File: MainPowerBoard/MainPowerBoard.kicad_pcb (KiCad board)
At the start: 2 copper layers, 177.8 x 177.8 mm, 255 parts, among them J101 CONN_01X04, J102 CONN_01X04, J103 CONN_01X04, J104 CONN_01X02, J105 CONN_01X02, J106 CONN_01X06, J107 CONN_01X06, J108 CONN_01X04, J109 CONN_01X04, J110 CONN_01X02, J111 CONN_01X02, J112 CONN_01X02, J113 CONN_01X02, J114 CONN_01X02, J115 CONN_01X02, J116 CONN_01X02, J117 CONN_01X02, J118 CONN_01X02, J119 CONN_01X02, J120 CONN_01X02, J121 CONN_01X02, J122 CONN_01X02, J123 CONN_01X02, J124 CONN_01X02, J125 CONN_01X02, J126 CONN_01X02, J127 CONN_01X04, J130 MOUNTING_HOLE, J131 MOUNTING_HOLE, J132 MOUNTING_HOLE, J133 MOUNTING_HOLE, Q101 FDB3632, Q401 FDB3632, Q501 FDB3632, Q601 FDB3632, SW701 KS-01Q-01, U1001 LMR16030S, U101 LTC4357MPMS8, U1101 LMR16030S, U1201 LMR16030S, U1301 LMR16030S, U1401 LMR16030S, U201 LMR16030S, U301 LMR16030S, U401 LTC4357MPMS8, U501 LTC4357MPMS8, U601 LTC4357MPMS8, U701 AP2204RA-5.0TRG1, U702 TLV271IDBVR, U703 LTC2950-1, U704 TLC393, U801 LMR16030S, U901 LMR16030S

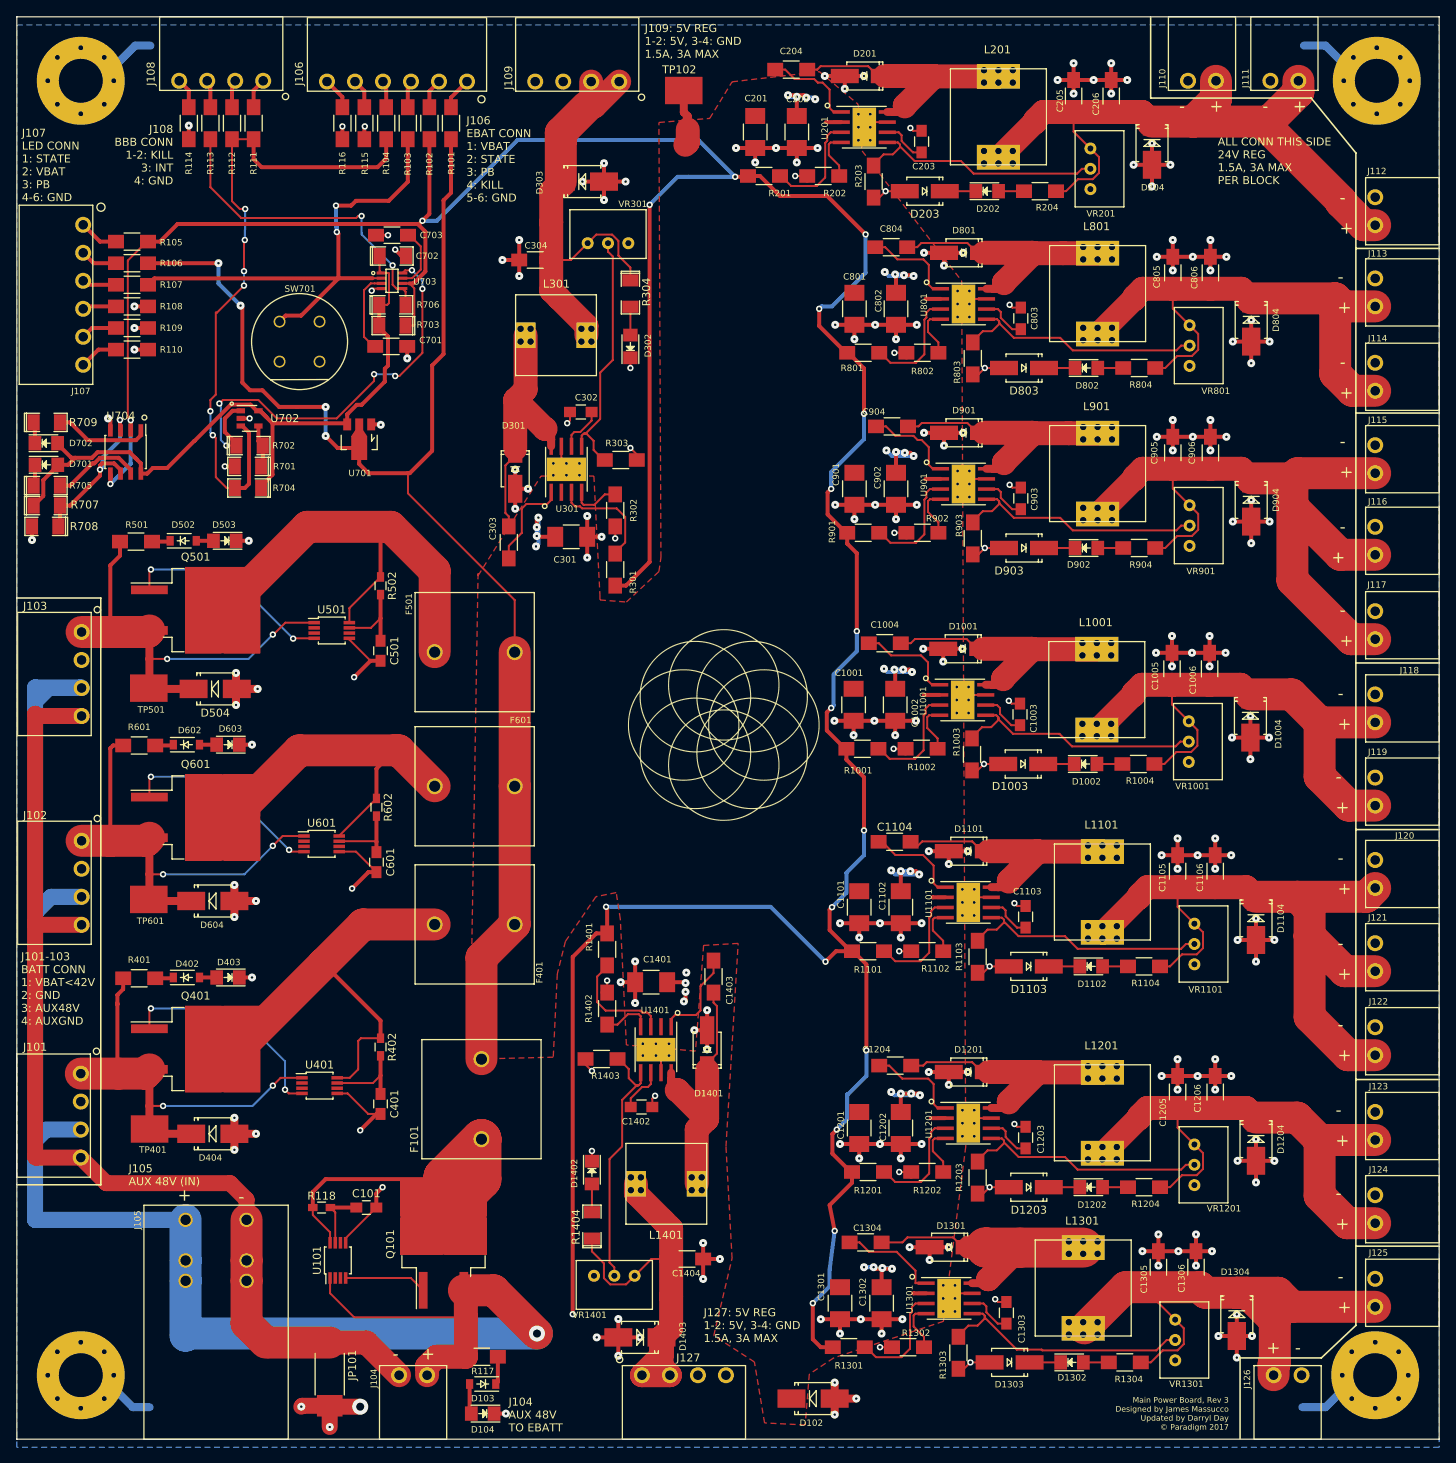
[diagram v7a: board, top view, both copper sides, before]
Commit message: Converted back to 8 24V rails on MPB, fixed NC pins on THBO schematic
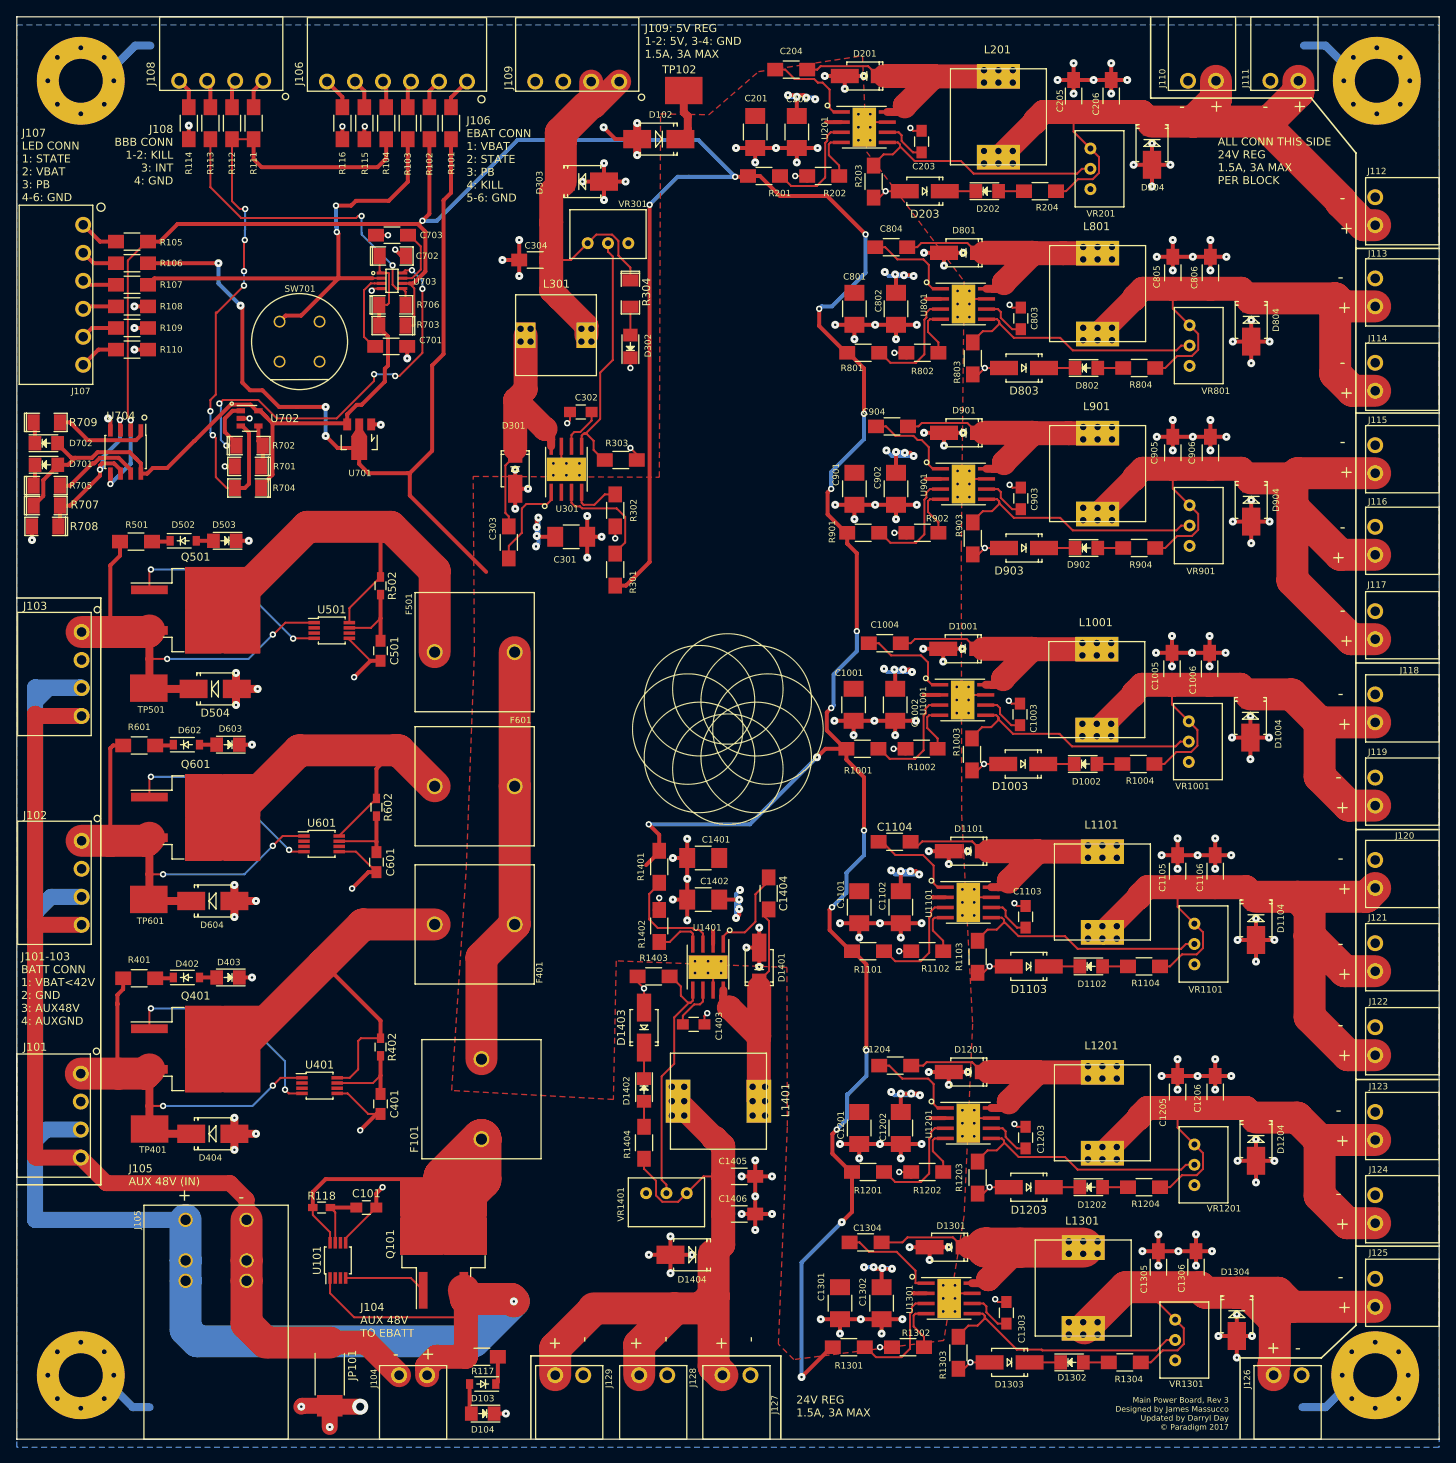
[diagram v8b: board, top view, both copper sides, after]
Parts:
- added C1405: 4.7uF, Capacitors_SMD:C_1206_HandSoldering, F.Cu at (90.3, 144.9)
- added C1406: 4.7uF, Capacitors_SMD:C_1206_HandSoldering, F.Cu at (90.3, 149.6)
- added D1404: 28V, Diodes_SMD:SMB_Handsoldering, F.Cu at (84.4, 154.7)
- added J128: CONN_01X02, hyperCustom:CONN_PHOENIX_1844210_2PIN, F.Cu at (75.4, 177.8)
- added J129: CONN_01X02, hyperCustom:CONN_PHOENIX_1844210_2PIN, F.Cu at (64.9, 177.8)
- C1402: footprint Resistors_SMD:R_0805_HandSoldering -> Capacitors_SMD:C_1210_HandSoldering
- C1403: value 0.1uF -> 2.2uF; footprint Resistors_SMD:R_1206_HandSoldering -> Resistors_SMD:R_0805_HandSoldering
- C1404: value 47uF -> 0.1uF; footprint Capacitors_SMD:C_1206_HandSoldering -> Resistors_SMD:R_1206_HandSoldering
- D1403: value 7.5V -> 18V; footprint Diodes_SMD:SMB_Handsoldering -> Diodes_SMD:SMA_Handsoldering
- J127: value CONN_01X04 -> CONN_01X02; footprint hyperCustom:CONN_PHOENIX_1844236_4PIN_1 -> hyperCustom:CONN_PHOENIX_1844210_2PIN
- L1401: value 15uH -> 47uH; footprint hyperCustom:15uIND_SLF10165T-150M3R13PF_BOURNS_heatsink -> hyperCustom:47uIND_CDRH127_LDNP-470MC_SUMIDA_heatsink
- R1403: value 12k -> 20k
- R1404: value 300 -> 400; footprint SMD_Packages:SMD-1206_Pol -> Resistors_SMD:R_1206_HandSoldering
- VR1401: value 100k -> 1M
- moved D102 158.6 mm to (80.2, 15.3), turned to 180 degrees
- moved C1404 46.8 mm to (94.0, 109.6), turned to 270 degrees
- moved D1403 38.7 mm to (78.4, 126.3), turned to 90 degrees
- moved C1402 27.0 mm to (85.8, 110.3), turned to 180 degrees
- moved C1401 16.8 mm to (85.8, 105.1)
- moved D1401 12.2 mm to (92.8, 118.8)
- moved L1401 12.2 mm to (87.7, 135.5), turned to 270 degrees
- moved R1402 12.2 mm to (80.3, 113.6)
- moved R1403 12.2 mm to (79.6, 119.9)
- moved R1404 12.2 mm to (78.4, 140.7)
- moved U1401 12.2 mm to (86.4, 118.8)
- moved VR1401 12.2 mm to (76.4, 151.2)
- moved R1401 12.2 mm to (80.3, 106.2)
- moved D1402 12.2 mm to (78.4, 134.1)
- moved J127 10.1 mm to (85.8, 177.8)
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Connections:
- C1402 pad 1: Net-(C1402-Pad1) -> /MAIN_POWER
- C1403 pad 2: Net-(C1403-Pad2) -> GND
- C1404 pad 1: /5V0_REG2 -> Net-(C1404-Pad1)
- C1404 pad 2: GND -> Net-(C1404-Pad2)
- D1401 pad 1: Net-(C1403-Pad2) -> Net-(C1404-Pad2)
- D1402 pad 1: GND -> Net-(D1402-Pad1)
- D1403 pad 1: /5V0_REG2 -> Net-(D1402-Pad1)
- J127 pad 1: /5V0_REG2 -> /24V0_REG8
- J127 pad 2: /5V0_REG2 -> GND
- L1401 pad 1: Net-(C1403-Pad2) -> Net-(C1404-Pad2)
- L1401 pad 2: /5V0_REG2 -> /24V0_REG8
- R1404 pad 1: /5V0_REG2 -> /24V0_REG8
- U1401 pad 1: Net-(C1403-Pad1) -> Net-(C1404-Pad1)
- U1401 pad 6: Net-(C1402-Pad1) -> Net-(C1403-Pad1)
- U1401 pad 8: Net-(C1403-Pad2) -> Net-(C1404-Pad2)
- VR1401 pad 3: /5V0_REG2 -> /24V0_REG8
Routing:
- net /24V0_REG8: track 0.00 -> 90.2 mm
- net /5V0_REG2: track 51.2 -> 0.00 mm
- net Net-(C1404-Pad2): track 0.00 -> 45.5 mm
- net /STATE: track 479.1 -> 434.3 mm, vias 20 -> 19
- net Net-(C1403-Pad2): track 32.9 -> 0.00 mm
- net GND: track 626.4 -> 646.1 mm, vias 228 -> 231
- net /MAIN_POWER: track 281.1 -> 268.3 mm, vias 37 -> 40
- net Net-(C1404-Pad1): track 0.00 -> 12.1 mm
- net Net-(C1403-Pad1): track 12.0 -> 5.76 mm
- net Net-(C1402-Pad1): track 5.76 -> 0.00 mm
- net /48V0_FROM_LINE_UNPROT: track 218.7 -> 213.4 mm
- net Net-(D1402-Pad1): track 0.00 -> 3.88 mm
- net (no net): track 1.28 -> 0.00 mm, vias 3 -> 0
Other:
- board text added: "24V REG 1.5A, 3A MAX"
- board text removed: "J127: 5V REG 1-2: 5V, 3-4: GND 1.5A, 3A MAX"
